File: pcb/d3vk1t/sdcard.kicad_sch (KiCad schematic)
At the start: 1 part, among them J1 Micro_SD_Card_Det

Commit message: [update all schematics sheets]
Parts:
- added C1: 1nF, Capacitor_SMD:C_1206_3216Metric, symbol Device:C_Small
- added R3: 10K, Resistor_SMD:R_0402_1005Metric, symbol Device:R_Small
- added R3: 1M, Resistor_SMD:R_1206_3216Metric, symbol Device:R_Small
- renumbered J1 to X
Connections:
- net at X.11 (SHIELD): now also C1.1, R3.2
- net +3.3V: now reaches X.4 (VDD)
- net +3.3V: now also R3.2
- net GND: now reaches X.6 (VSS)
- net GND: now also C1.2, R3.1
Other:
- moved on the sheet: X
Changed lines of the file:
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@@
 (kicad_sch (version 20230121) (generator eeschema)
   (paper "A4")
-  (symbol (lib_id "db-sdcard:Micro_SD_Card_Det") (at 186.69 100.838 0) (mirror y) (unit 1)
-    (in_bom yes) (on_board yes) (dnp no) (fields_autoplaced)
-    (property "Reference" "J1" (at 186.69 83.82 0)
-      (effects (font (size 1.27 1.27)))
-    )
-    (property "Value" "Micro_SD_Card_Det" (at 186.69 86.36 0)
-      (effects (font (size 1.27 1.27)))
-    )
-    (property "Footprint" "db:microSD_SOFNG_TF-015" (at 134.62 83.058 0)
-      (effects (font (size 1.27 1.27)) hide)
-    )
-    (property "Datasheet" "https://www.hirose.com/product/en/download_file/key_name/DM3/category/Catalog/doc_file_id/49662/?file_category_id=4&item_id=195&is_series=1" (at 187.96 117.348 0)
+  (junction (at 195.58 127) (diameter 0) (color 0 0 0 0)
+  )
+  (junction (at 195.58 114.3) (diameter 0) (color 0 0 0 0)
+  )
+  (wire (pts (xy 137.16 124.46) (xy 137.16 127))
+    (stroke (width 0) (type default))
+  )
+  (wire (pts (xy 187.96 96.52) (xy 193.04 96.52))
+    (stroke (width 0) (type default))
+  )
+  (wire (pts (xy 195.58 127) (xy 190.5 127))
+    (stroke (width 0) (type default))
+  )
+  (wire (pts (xy 203.2 124.46) (xy 203.2 127))
+    (stroke (width 0) (type default))
+  )
+  (wire (pts (xy 193.04 93.98) (xy 193.04 96.52))
+    (stroke (width 0) (type default))
+  )
+  (wire (pts (xy 195.58 124.46) (xy 195.58 127))
+    (stroke (width 0) (type default))
+  )
+  (wire (pts (xy 195.58 127) (xy 195.58 129.54))
+    (stroke (width 0) (type default))
+  )
+  (wire (pts (xy 187.96 116.84) (xy 190.5 116.84))
+    (stroke (width 0) (type default))
+  )
+  (wire (pts (xy 203.2 114.3) (xy 203.2 119.38))
+    (stroke (width 0) (type default))
+  )
+  (wire (pts (xy 190.5 116.84) (xy 190.5 127))
+    (stroke (width 0) (type default))
+  )
+  (wire (pts (xy 195.58 114.3) (xy 203.2 114.3))
+    (stroke (width 0) (type default))
+  )
+  (wire (pts (xy 195.58 119.38) (xy 195.58 114.3))
+    (stroke (width 0) (type default))
+  )
+  (wire (pts (xy 195.58 114.3) (xy 187.96 114.3))
+    (stroke (width 0) (type default))
+  )
+  (wire (pts (xy 203.2 127) (xy 195.58 127))
+    (stroke (width 0) (type default))
+  )
+  (symbol (lib_id "power:+3.3V") (at 193.04 93.98 0) (unit 1)
+    (in_bom yes) (on_board yes) (dnp no) (fields_autoplaced)
+    (property "Reference" "#PWR02" (at 193.04 97.79 0)
+      (effects (font (size 1.27 1.27)) hide)
+    )
+    (property "Value" "+3.3V" (at 193.04 90.17 0)
+      (effects (font (size 1.27 1.27)))
+    )
+    (property "Footprint" "" (at 193.04 93.98 0)
+      (effects (font (size 1.27 1.27)) hide)
+    )
+    (property "Datasheet" "" (at 193.04 93.98 0)
+      (effects (font (size 1.27 1.27)) hide)
+    )
+    (pin "1")
+    (instances
+      (project "d3vk1t"
+        (path "/4ea523ae-7c45-478e-a9cc-6f4833d1a9d5/0c7e2350-c710-4f8b-bffc-99ae7438d4de"
+          (reference "#PWR02") (unit 1)
+        )
+        (path "/4ea523ae-7c45-478e-a9cc-6f4833d1a9d5/41f8e312-86c0-4917-8944-524577576fad"
+          (reference "#PWR014") (unit 1)
+        )
+        (path "/4ea523ae-7c45-478e-a9cc-6f4833d1a9d5/aea6c2ba-3179-4867-b0ce-0dd87f8d3618"
+          (reference "#PWR027") (unit 1)
+        )
+      )
+    )
+  )
+  (symbol (lib_id "power:+3.3V") (at 137.16 124.46 0) (unit 1)
+    (in_bom yes) (on_board yes) (dnp no) (fields_autoplaced)
+    (property "Reference" "#PWR02" (at 137.16 128.27 0)
+      (effects (font (size 1.27 1.27)) hide)
+    )
+    (property "Value" "+3.3V" (at 137.16 120.65 0)
+      (effects (font (size 1.27 1.27)))
+    )
+    (property "Footprint" "" (at 137.16 124.46 0)
+      (effects (font (size 1.27 1.27)) hide)
+    )
+    (property "Datasheet" "" (at 137.16 124.46 0)
+      (effects (font (size 1.27 1.27)) hide)
+    )
+    (pin "1")
+    (instances
+      (project "d3vk1t"
+        (path "/4ea523ae-7c45-478e-a9cc-6f4833d1a9d5/0c7e2350-c710-4f8b-bffc-99ae7438d4de"
+          (reference "#PWR02") (unit 1)
+        )
+        (path "/4ea523ae-7c45-478e-a9cc-6f4833d1a9d5/41f8e312-86c0-4917-8944-524577576fad"
+          (reference "#PWR012") (unit 1)
+        )
+        (path "/4ea523ae-7c45-478e-a9cc-6f4833d1a9d5/aea6c2ba-3179-4867-b0ce-0dd87f8d3618"
+          (reference "#PWR050") (unit 1)
+        )
+      )
+    )
+  )
+  (symbol (lib_id "db-sdcard:Micro_SD_Card_Det") (at 175.26 106.68 0) (mirror y) (unit 1)
+    (in_bom yes) (on_board yes) (dnp no)
+    (property "Reference" "X" (at 166.37 92.202 0)
+      (effects (font (size 1.27 1.27)))
+    )
+    (property "Value" "Micro_SD_Card_Det" (at 175.26 92.202 0)
+      (effects (font (size 1.27 1.27)) hide)
+    )
+    (property "Footprint" "db:microSD_SOFNG_TF-015" (at 123.19 88.9 0)
+      (effects (font (size 1.27 1.27)) hide)
+    )
+    (property "Datasheet" "https://www.hirose.com/product/en/download_file/key_name/DM3/category/Catalog/doc_file_id/49662/?file_category_id=4&item_id=195&is_series=1" (at 176.53 123.19 0)
       (effects (font (size 1.27 1.27)) hide)
     )
@@
       (project "d3vk1t"
         (path "/4ea523ae-7c45-478e-a9cc-6f4833d1a9d5/aea6c2ba-3179-4867-b0ce-0dd87f8d3618"
-          (reference "J1") (unit 1)
-        )
-      )
+          (reference "X") (unit 1)
+        )
+      )
+    )
+  )
+  (symbol (lib_id "Device:C_Small") (at 203.2 121.92 0) (unit 1)
+    (in_bom yes) (on_board yes) (dnp no) (fields_autoplaced)
+    (property "Reference" "C1" (at 205.994 121.2913 0)
+      (effects (font (size 1.27 1.27)) (justify left))
+    )
+    (property "Value" "1nF" (at 205.994 123.8313 0)
+      (effects (font (size 1.27 1.27)) (justify left))
+    )
+    (property "Footprint" "Capacitor_SMD:C_1206_3216Metric" (at 203.2 121.92 0)
+      (effects (font (size 1.27 1.27)) hide)
+    )
+    (property "Datasheet" "~" (at 203.2 121.92 0)
+      (effects (font (size 1.27 1.27)) hide)
+    )
+    (pin "1")
+    (pin "2")
+    (instances
+      (project "d3vk1t"
+        (path "/4ea523ae-7c45-478e-a9cc-6f4833d1a9d5/0c7e2350-c710-4f8b-bffc-99ae7438d4de"
+          (reference "C1") (unit 1)
+        )
+        (path "/4ea523ae-7c45-478e-a9cc-6f4833d1a9d5/41f8e312-86c0-4917-8944-524577576fad"
+          (reference "C12") (unit 1)
+        )
+        (path "/4ea523ae-7c45-478e-a9cc-6f4833d1a9d5/fd7cf4b0-4d20-445a-8ab6-186a5df83da1"
+          (reference "C13") (unit 1)
+        )
+        (path "/4ea523ae-7c45-478e-a9cc-6f4833d1a9d5/aea6c2ba-3179-4867-b0ce-0dd87f8d3618"
+          (reference "C14") (unit 1)
+        )
+      )
+    )
+  )
+  (symbol (lib_id "power:GND") (at 195.58 129.54 0) (unit 1)
+    (in_bom yes) (on_board yes) (dnp no) (fields_autoplaced)
+    (property "Reference" "#PWR026" (at 195.58 135.89 0)
+      (effects (font (size 1.27 1.27)) hide)
+    )
+    (property "Value" "GND" (at 195.58 134.62 0)
+      (effects (font (size 1.27 1.27)))
+    )
+    (property "Footprint" "" (at 195.58 129.54 0)
+      (effects (font (size 1.27 1.27)) hide)
+    )
+    (property "Datasheet" "" (at 195.58 129.54 0)
+      (effects (font (size 1.27 1.27)) hide)
+    )
+    (pin "1")
+    (instances
+      (project "d3vk1t"
+        (path "/4ea523ae-7c45-478e-a9cc-6f4833d1a9d5/aea6c2ba-3179-4867-b0ce-0dd87f8d3618"
+          (reference "#PWR026") (unit 1)
+        )
+      )
+    )
+  )
+  (symbol (lib_id "Device:R_Small") (at 137.16 129.54 180) (unit 1)
+    (in_bom yes) (on_board yes) (dnp no)
+    (property "Reference" "R3" (at 134.62 129.54 90)
+      (effects (font (size 1.27 1.27)))
+    )
+    (property "Value" "10K" (at 139.7 129.54 90)
+      (effects (font (size 1.27 1.27)))
+    )
+    (property "Footprint" "Resistor_SMD:R_0402_1005Metric" (at 137.16 129.54 0)
+      (effects (font (size 1.27 1.27)) hide)
+    )
+    (property "Datasheet" "~" (at 137.16 129.54 0)
+      (effects (font (size 1.27 1.27)) hide)
+    )
+    (pin "1")
+    (pin "2")
+    (instances
+      (project "d3vk1t"
+        (path "/4ea523ae-7c45-478e-a9cc-6f4833d1a9d5/41f8e312-86c0-4917-8944-524577576fad"
+          (reference "R3") (unit 1)
+        )
+        (path "/4ea523ae-7c45-478e-a9cc-6f4833d1a9d5/aea6c2ba-3179-4867-b0ce-0dd87f8d3618"
+          (reference "R15") (unit 1)
+        )
+      )
+    )
+  )
+  (symbol (lib_id "Device:R_Small") (at 195.58 121.92 180) (unit 1)
+    (in_bom yes) (on_board yes) (dnp no)
+    (property "Reference" "R3" (at 193.04 121.92 90)
+      (effects (font (size 1.27 1.27)))
+    )
+    (property "Value" "1M" (at 198.12 121.92 90)
+      (effects (font (size 1.27 1.27)))
+    )
+    (property "Footprint" "Resistor_SMD:R_1206_3216Metric" (at 195.58 121.92 0)
+      (effects (font (size 1.27 1.27)) hide)
+    )
+    (property "Datasheet" "~" (at 195.58 121.92 0)
+      (effects (font (size 1.27 1.27)) hide)
+    )
+    (pin "1")
+    (pin "2")
+    (instances
+      (project "d3vk1t"
+        (path "/4ea523ae-7c45-478e-a9cc-6f4833d1a9d5/41f8e312-86c0-4917-8944-524577576fad"
+          (reference "R3") (unit 1)
+        )
+        (path "/4ea523ae-7c45-478e-a9cc-6f4833d1a9d5/fd7cf4b0-4d20-445a-8ab6-186a5df83da1"
+          (reference "R6") (unit 1)
+        )
+        (path "/4ea523ae-7c45-478e-a9cc-6f4833d1a9d5/aea6c2ba-3179-4867-b0ce-0dd87f8d3618"
+          (reference "R9") (unit 1)
+        )
+      )

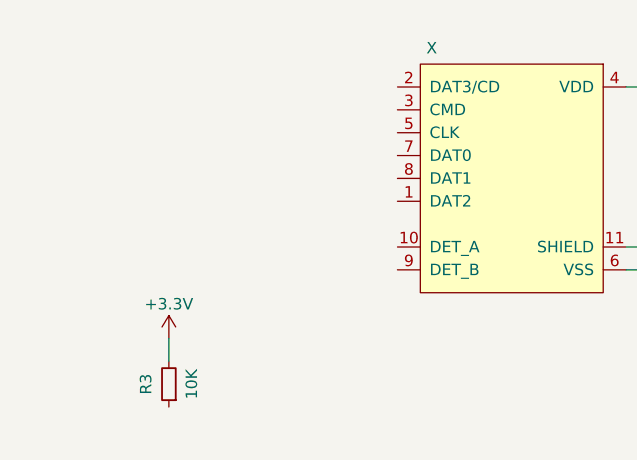
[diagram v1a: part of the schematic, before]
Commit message: sch: update all sch sheets.
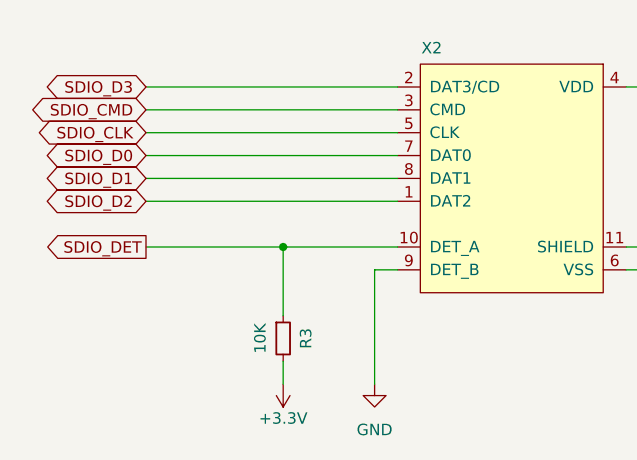
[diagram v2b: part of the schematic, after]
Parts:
- renumbered X to X2
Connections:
- net GND: now also X2.9 (DET_B)
- net SDIO_D2: now reaches X2.1 (DAT2)
- net SDIO_DET: now reaches X2.10 (DET_A)
- net SDIO_DET: now also R3.1
- net SDIO_D3: now reaches X2.2 (DAT3/CD)
- net SDIO_CMD: now reaches X2.3 (CMD)
- net SDIO_CLK: now reaches X2.5 (CLK)
- net SDIO_D0: now reaches X2.7 (DAT0)
- net SDIO_D1: now reaches X2.8 (DAT1)
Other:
- moved on the sheet: R3
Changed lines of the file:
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@@
   (junction (at 195.58 127) (diameter 0) (color 0 0 0 0)
   )
+  (junction (at 149.86 114.3) (diameter 0) (color 0 0 0 0)
+  )
   (junction (at 195.58 114.3) (diameter 0) (color 0 0 0 0)
   )
-  (wire (pts (xy 137.16 124.46) (xy 137.16 127))
+  (wire (pts (xy 149.86 129.54) (xy 149.86 127))
     (stroke (width 0) (type default))
   )
@@
     (stroke (width 0) (type default))
   )
+  (wire (pts (xy 160.02 129.54) (xy 160.02 116.84))
+    (stroke (width 0) (type default))
+  )
+  (wire (pts (xy 160.02 116.84) (xy 162.56 116.84))
+    (stroke (width 0) (type default))
+  )
+  (wire (pts (xy 134.62 101.6) (xy 162.56 101.6))
+    (stroke (width 0) (type default))
+  )
+  (wire (pts (xy 134.62 99.06) (xy 162.56 99.06))
+    (stroke (width 0) (type default))
+  )
   (wire (pts (xy 203.2 124.46) (xy 203.2 127))
     (stroke (width 0) (type default))
@@
     (stroke (width 0) (type default))
   )
+  (wire (pts (xy 134.62 109.22) (xy 162.56 109.22))
+    (stroke (width 0) (type default))
+  )
+  (wire (pts (xy 134.62 104.14) (xy 162.56 104.14))
+    (stroke (width 0) (type default))
+  )
+  (wire (pts (xy 134.62 106.68) (xy 162.56 106.68))
+    (stroke (width 0) (type default))
+  )
   (wire (pts (xy 187.96 116.84) (xy 190.5 116.84))
     (stroke (width 0) (type default))
@@
     (stroke (width 0) (type default))
   )
+  (wire (pts (xy 134.62 114.3) (xy 149.86 114.3))
+    (stroke (width 0) (type default))
+  )
   (wire (pts (xy 190.5 116.84) (xy 190.5 127))
     (stroke (width 0) (type default))
   )
+  (wire (pts (xy 134.62 96.52) (xy 162.56 96.52))
+    (stroke (width 0) (type default))
+  )
   (wire (pts (xy 195.58 114.3) (xy 203.2 114.3))
     (stroke (width 0) (type default))
@@
     (stroke (width 0) (type default))
   )
+  (wire (pts (xy 149.86 114.3) (xy 162.56 114.3))
+    (stroke (width 0) (type default))
+  )
   (wire (pts (xy 203.2 127) (xy 195.58 127))
     (stroke (width 0) (type default))
+  )
+  (wire (pts (xy 149.86 121.92) (xy 149.86 114.3))
+    (stroke (width 0) (type default))
+  )
+  (global_label "SDIO_D3" (shape bidirectional) (at 134.62 96.52 180) (fields_autoplaced)
+    (effects (font (size 1.27 1.27)) (justify right))
+    (property "Intersheetrefs" "${INTERSHEET_REFS}" (at 122.741 96.52 0)
+      (effects (font (size 1.27 1.27)) (justify right) hide)
+    )
+  )
+  (global_label "SDIO_D0" (shape bidirectional) (at 134.62 104.14 180) (fields_autoplaced)
+    (effects (font (size 1.27 1.27)) (justify right))
+    (property "Intersheetrefs" "${INTERSHEET_REFS}" (at 122.741 104.14 0)
+      (effects (font (size 1.27 1.27)) (justify right) hide)
+    )
+  )
+  (global_label "SDIO_D1" (shape bidirectional) (at 134.62 106.68 180) (fields_autoplaced)
+    (effects (font (size 1.27 1.27)) (justify right))
+    (property "Intersheetrefs" "${INTERSHEET_REFS}" (at 122.741 106.68 0)
+      (effects (font (size 1.27 1.27)) (justify right) hide)
+    )
+  )
+  (global_label "SDIO_CLK" (shape bidirectional) (at 134.62 101.6 180) (fields_autoplaced)
+    (effects (font (size 1.27 1.27)) (justify right))
+    (property "Intersheetrefs" "${INTERSHEET_REFS}" (at 121.6524 101.6 0)
+      (effects (font (size 1.27 1.27)) (justify right) hide)
+    )
+  )
+  (global_label "SDIO_CMD" (shape bidirectional) (at 134.62 99.06 180) (fields_autoplaced)
+    (effects (font (size 1.27 1.27)) (justify right))
+    (property "Intersheetrefs" "${INTERSHEET_REFS}" (at 121.2291 99.06 0)
+      (effects (font (size 1.27 1.27)) (justify right) hide)
+    )
+  )
+  (global_label "SDIO_DET" (shape output) (at 134.62 114.3 180) (fields_autoplaced)
+    (effects (font (size 1.27 1.27)) (justify right))
+    (property "Intersheetrefs" "${INTERSHEET_REFS}" (at 122.9452 114.3 0)
+      (effects (font (size 1.27 1.27)) (justify right) hide)
+    )
+  )
+  (global_label "SDIO_D2" (shape bidirectional) (at 134.62 109.22 180) (fields_autoplaced)
+    (effects (font (size 1.27 1.27)) (justify right))
+    (property "Intersheetrefs" "${INTERSHEET_REFS}" (at 122.741 109.22 0)
+      (effects (font (size 1.27 1.27)) (justify right) hide)
+    )
   )
   (symbol (lib_id "power:+3.3V") (at 193.04 93.98 0) (unit 1)
@@
     )
   )
-  (symbol (lib_id "power:+3.3V") (at 137.16 124.46 0) (unit 1)
-    (in_bom yes) (on_board yes) (dnp no) (fields_autoplaced)
-    (property "Reference" "#PWR02" (at 137.16 128.27 0)
-      (effects (font (size 1.27 1.27)) hide)
-    )
-    (property "Value" "+3.3V" (at 137.16 120.65 0)
-      (effects (font (size 1.27 1.27)))
-    )
-    (property "Footprint" "" (at 137.16 124.46 0)
-      (effects (font (size 1.27 1.27)) hide)
-    )
-    (property "Datasheet" "" (at 137.16 124.46 0)
+  (symbol (lib_id "power:+3.3V") (at 149.86 129.54 180) (unit 1)
+    (in_bom yes) (on_board yes) (dnp no) (fields_autoplaced)
+    (property "Reference" "#PWR02" (at 149.86 125.73 0)
+      (effects (font (size 1.27 1.27)) hide)
+    )
+    (property "Value" "+3.3V" (at 149.86 133.35 0)
+      (effects (font (size 1.27 1.27)))
+    )
+    (property "Footprint" "" (at 149.86 129.54 0)
+      (effects (font (size 1.27 1.27)) hide)
+    )
+    (property "Datasheet" "" (at 149.86 129.54 0)
       (effects (font (size 1.27 1.27)) hide)
     )
@@
   (symbol (lib_id "db-sdcard:Micro_SD_Card_Det") (at 175.26 106.68 0) (mirror y) (unit 1)
     (in_bom yes) (on_board yes) (dnp no)
-    (property "Reference" "X" (at 166.37 92.202 0)
+    (property "Reference" "X2" (at 166.37 92.202 0)
       (effects (font (size 1.27 1.27)))
     )
@@
       (project "d3vk1t"
         (path "/4ea523ae-7c45-478e-a9cc-6f4833d1a9d5/aea6c2ba-3179-4867-b0ce-0dd87f8d3618"
-          (reference "X") (unit 1)
+          (reference "X2") (unit 1)
         )
       )
@@
     )
   )
+  (symbol (lib_id "power:GND") (at 160.02 129.54 0) (unit 1)
+    (in_bom yes) (on_board yes) (dnp no) (fields_autoplaced)
+    (property "Reference" "#PWR054" (at 160.02 135.89 0)
+      (effects (font (size 1.27 1.27)) hide)
+    )
+    (property "Value" "GND" (at 160.02 134.62 0)
+      (effects (font (size 1.27 1.27)))
+    )
+    (property "Footprint" "" (at 160.02 129.54 0)
+      (effects (font (size 1.27 1.27)) hide)
+    )
+    (property "Datasheet" "" (at 160.02 129.54 0)
+      (effects (font (size 1.27 1.27)) hide)
+    )
+    (pin "1")
+    (instances
+      (project "d3vk1t"
+        (path "/4ea523ae-7c45-478e-a9cc-6f4833d1a9d5/aea6c2ba-3179-4867-b0ce-0dd87f8d3618"
+          (reference "#PWR054") (unit 1)
+        )
+      )
+    )
+  )
   (symbol (lib_id "power:GND") (at 195.58 129.54 0) (unit 1)
     (in_bom yes) (on_board yes) (dnp no) (fields_autoplaced)
@@
     )
   )
-  (symbol (lib_id "Device:R_Small") (at 137.16 129.54 180) (unit 1)
+  (symbol (lib_id "Device:R_Small") (at 149.86 124.46 0) (unit 1)
     (in_bom yes) (on_board yes) (dnp no)
-    (property "Reference" "R3" (at 134.62 129.54 90)
-      (effects (font (size 1.27 1.27)))
-    )
-    (property "Value" "10K" (at 139.7 129.54 90)
-      (effects (font (size 1.27 1.27)))
-    )
-    (property "Footprint" "Resistor_SMD:R_0402_1005Metric" (at 137.16 129.54 0)
-      (effects (font (size 1.27 1.27)) hide)
-    )
-    (property "Datasheet" "~" (at 137.16 129.54 0)
-      (effects (font (size 1.27 1.27)) hide)
-    )
+    (property "Reference" "R3" (at 152.4 124.46 90)
+      (effects (font (size 1.27 1.27)))
+    )
+    (property "Value" "10K" (at 147.32 124.46 90)
+      (effects (font (size 1.27 1.27)))
+    )
+    (property "Footprint" "Resistor_SMD:R_0402_1005Metric" (at 149.86 124.46 0)
+      (effects (font (size 1.27 1.27)) hide)
+    )
+    (property "Datasheet" "~" (at 149.86 124.46 0)
+      (effects (font (size 1.27 1.27)) hide)
+    )

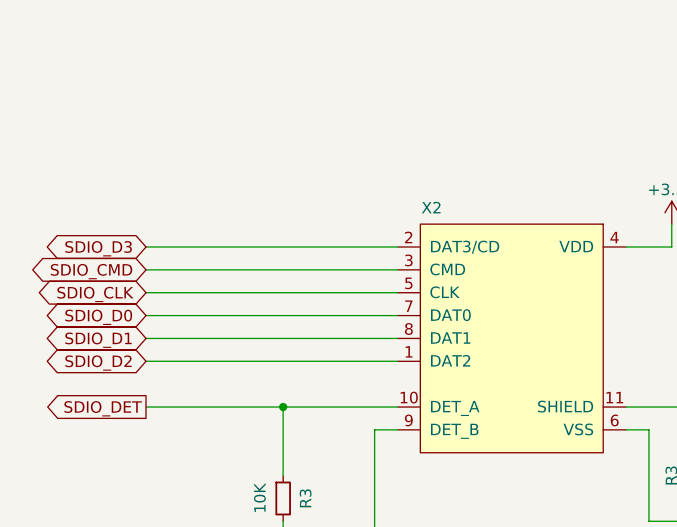
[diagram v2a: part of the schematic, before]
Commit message: pcb: update layout
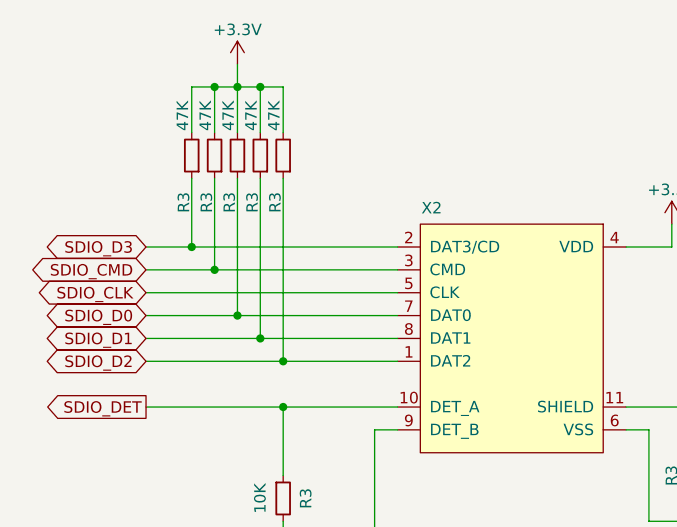
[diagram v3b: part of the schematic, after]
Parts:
- added R3 (x5): 47K, Resistor_SMD:R_0402_1005Metric, symbol Device:R_Small
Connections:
- net +3.3V: now also R3.2, R3.2, R3.2, R3.2, R3.2
- net SDIO_CMD: now also R3.1
- net SDIO_D0: now also R3.1
- net SDIO_D1: now also R3.1
- net SDIO_D2: now also R3.1
- net SDIO_D3: now also R3.1

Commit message: project update  - update pcb layout.  - update schmatics sheets.  - added manufacturing files.  - added documentation files.
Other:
- note added: "SDCARD CIRCUIT"
- title: (none) -> SDCard
- moved on the sheet: C1, R3, X2
